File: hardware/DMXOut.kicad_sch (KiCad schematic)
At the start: 3 parts, among them J201 SJ2-25404B-SMT-TR, U201 THVD24x2

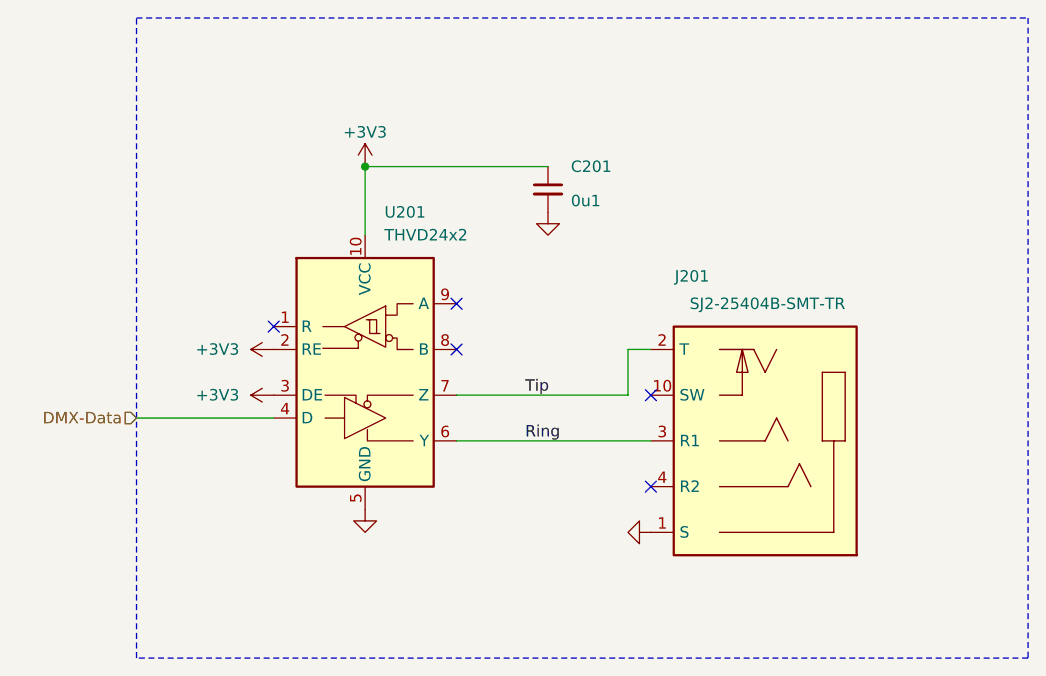
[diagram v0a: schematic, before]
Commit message: Update symbols
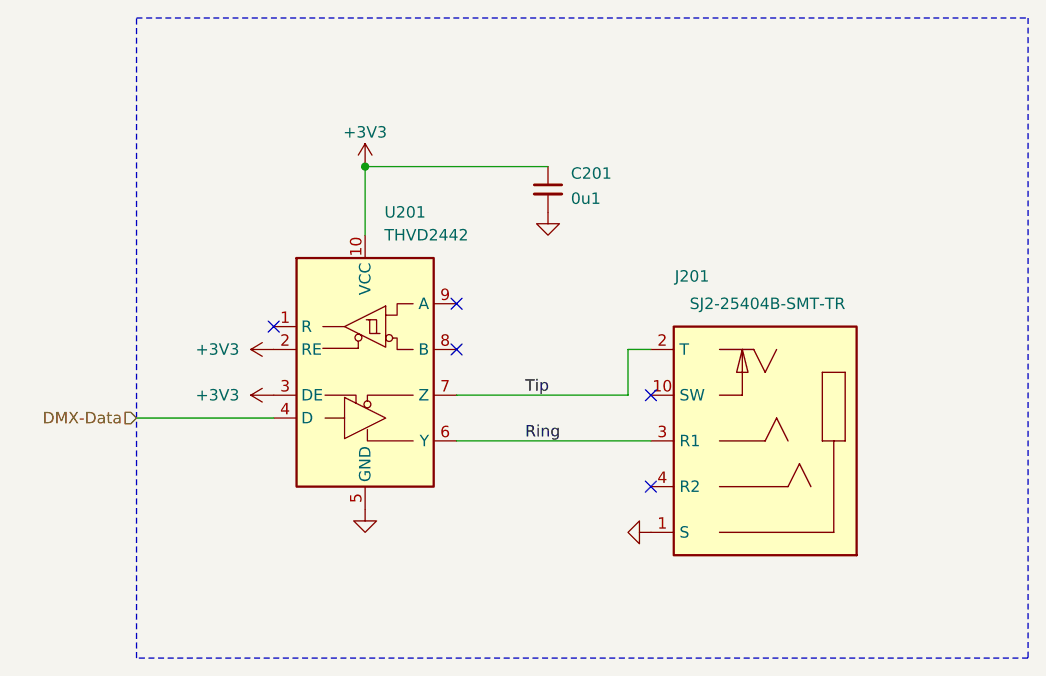
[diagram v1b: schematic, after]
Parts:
- C201: footprint Capacitor_SMD:C_0603_1608Metric -> V2_Capacitor_SMD:C_0603; symbol Device:C_Small -> V2_Device:C_0603_0u1; Mouser (none) -> 810-CGA3E2X7R1H104MA
- J201: Mouser (none) -> 490-SJ2-25404BSMT-TR
- U201: value THVD24x2 -> THVD2442; symbol V2_Interface_RS485:THVD24x2 -> V2_Interface_RS485:THVD2442; Mouser (none) -> 595-THVD2442DRCR
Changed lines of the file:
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@@
 			)
 		)
-		(property "Description" ""
+		(property "Description" "Power symbol creates a global label with name \"GND\" , ground"
 			(at 128.27 125.73 0)
 			(effects
@@
 	)
 	(symbol
-		(lib_id "V2_Interface_RS485:THVD24x2")
+		(lib_id "V2_Interface_RS485:THVD2442")
 		(at 128.27 110.49 0)
 		(unit 1)
@@
 			)
 		)
-		(property "Value" "THVD24x2"
+		(property "Value" "THVD2442"
 			(at 130.4133 95.25 0)
 			(effects
@@
 		)
 		(property "Description" ""
+			(at 128.27 110.49 0)
+			(effects
+				(font
+					(size 1.27 1.27)
+				)
+				(hide yes)
+			)
+		)
+		(property "Mouser" " 595-THVD2442DRCR "
 			(at 128.27 110.49 0)
 			(effects
@@
 			)
 		)
-		(property "Description" ""
+		(property "Description" "Power symbol creates a global label with name \"+3V3\""
 			(at 128.27 87.63 0)
 			(effects
@@
 			)
 		)
-		(property "Description" ""
+		(property "Description" "Power symbol creates a global label with name \"GND\" , ground"
 			(at 160.02 128.27 0)
 			(effects
@@
 			)
 		)
-		(property "Description" ""
+		(property "Description" "Power symbol creates a global label with name \"+3V3\""
 			(at 118.11 107.95 0)
 			(effects
@@
 			)
 		)
+		(property "Mouser" " 490-SJ2-25404BSMT-TR"
+			(at 172.72 118.11 0)
+			(effects
+				(font
+					(size 1.27 1.27)
+				)
+				(hide yes)
+			)
+		)
 		(pin "1"
 		)
@@
 	)
 	(symbol
-		(lib_id "Device:C_Small")
+		(lib_id "V2_Device:C_0603_0u1")
 		(at 148.59 90.17 0)
 		(unit 1)
@@
 		(dnp no)
 		(property "Reference" "C201"
-			(at 151.13 87.6362 0)
+			(at 151.13 88.392 0)
 			(effects
 				(font
@@
 		)
 		(property "Value" "0u1"
-			(at 151.13 91.4462 0)
+			(at 151.13 91.186 0)
 			(effects
 				(font
@@
 			)
 		)
-		(property "Footprint" "Capacitor_SMD:C_0603_1608Metric"
+		(property "Footprint" "V2_Capacitor_SMD:C_0603"
+			(at 148.59 107.188 0)
+			(effects
+				(font
+					(size 1.27 1.27)
+				)
+				(hide yes)
+			)
+		)
+		(property "Datasheet" ""
 			(at 148.59 90.17 0)
 			(effects
@@
 			)
 		)
-		(property "Datasheet" "~"
-			(at 148.59 90.17 0)
-			(effects
-				(font
-					(size 1.27 1.27)
-				)
-				(hide yes)
-			)
-		)
-		(property "Description" ""
-			(at 148.59 90.17 0)
+		(property "Description" "Unpolarized capacitor, small symbol"
+			(at 148.59 103.632 0)
+			(effects
+				(font
+					(size 1.27 1.27)
+				)
+				(hide yes)
+			)
+		)
+		(property "Mouser" " 810-CGA3E2X7R1H104MA"
+			(at 148.59 110.49 0)
 			(effects
 				(font
@@
 			)
 		)
-		(property "Description" ""
+		(property "Description" "Power symbol creates a global label with name \"GND\" , ground"
 			(at 148.59 92.71 0)
 			(effects
@@
 			)
 		)
-		(property "Description" ""
+		(property "Description" "Power symbol creates a global label with name \"+3V3\""
 			(at 118.11 113.03 0)
 			(effects

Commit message: Refresh
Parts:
- C201: Mouser 810-CGA3E2X7R1H104MA -> 810-CGA3E2X7R1H104MA
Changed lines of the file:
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@@
 			)
 		)
-		(property "Mouser" " 810-CGA3E2X7R1H104MA"
+		(property "Mouser" "810-CGA3E2X7R1H104MA"
 			(at 148.59 110.49 0)
 			(effects

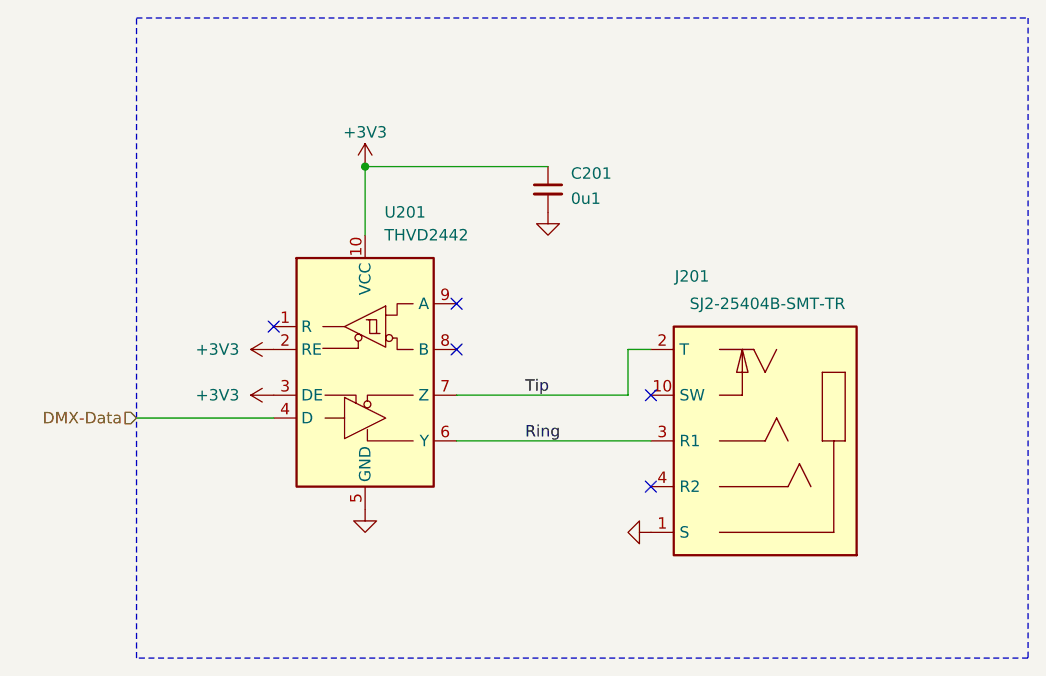
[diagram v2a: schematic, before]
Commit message: Update power symbols
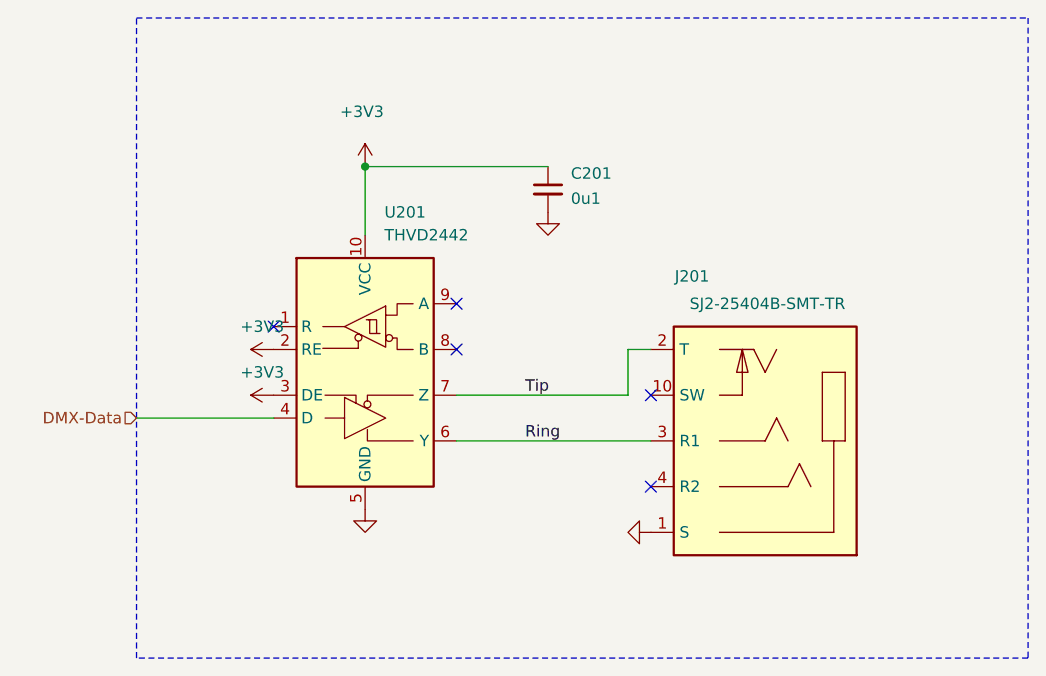
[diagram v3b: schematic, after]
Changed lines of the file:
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@@
 	)
 	(symbol
-		(lib_id "power:GND")
+		(lib_id "V2_power:GND")
 		(at 128.27 125.73 0)
 		(unit 1)
@@
 		)
 		(property "Value" "GND"
-			(at 128.27 130.81 0)
+			(at 128.27 129.794 0)
 			(effects
 				(font
@@
 		)
 		(property "Description" "Power symbol creates a global label with name \"GND\" , ground"
-			(at 128.27 125.73 0)
+			(at 128.016 136.144 0)
 			(effects
 				(font
@@
 	)
 	(symbol
-		(lib_id "power:+3V3")
+		(lib_id "V2_power:+3V3")
 		(at 128.27 87.63 0)
 		(unit 1)
@@
 		(on_board yes)
 		(dnp no)
-		(fields_autoplaced yes)
 		(property "Reference" "#PWR0201"
 			(at 128.27 91.44 0)
@@
 		)
 		(property "Value" "+3V3"
-			(at 128.27 83.82 0)
-			(effects
-				(font
-					(size 1.27 1.27)
-				)
+			(at 125.476 81.534 0)
+			(effects
+				(font
+					(size 1.27 1.27)
+				)
+				(justify left)
 			)
 		)
@@
 		)
 		(property "Description" "Power symbol creates a global label with name \"+3V3\""
-			(at 128.27 87.63 0)
+			(at 128.27 102.616 0)
 			(effects
 				(font
@@
 	)
 	(symbol
-		(lib_id "power:GND")
+		(lib_id "V2_power:GND")
 		(at 160.02 128.27 270)
 		(unit 1)
@@
 		)
 		(property "Value" "GND"
-			(at 156.21 128.2699 90)
-			(effects
-				(font
-					(size 1.27 1.27)
-				)
-				(justify right)
+			(at 155.956 128.27 0)
+			(effects
+				(font
+					(size 1.27 1.27)
+				)
 				(hide yes)
 			)
@@
 		)
 		(property "Description" "Power symbol creates a global label with name \"GND\" , ground"
-			(at 160.02 128.27 0)
+			(at 149.606 128.016 0)
 			(effects
 				(font
@@
 	)
 	(symbol
-		(lib_id "power:+3V3")
+		(lib_id "V2_power:+3V3")
 		(at 118.11 107.95 90)
 		(unit 1)
@@
 		)
 		(property "Value" "+3V3"
-			(at 114.3 107.9499 90)
-			(effects
-				(font
-					(size 1.27 1.27)
-				)
-				(justify left)
+			(at 116.84 105.41 90)
+			(effects
+				(font
+					(size 1.27 1.27)
+				)
 			)
 		)
@@
 		)
 		(property "Description" "Power symbol creates a global label with name \"+3V3\""
-			(at 118.11 107.95 0)
+			(at 133.096 107.95 0)
 			(effects
 				(font
@@
 	)
 	(symbol
-		(lib_id "power:GND")
+		(lib_id "V2_power:GND")
 		(at 148.59 92.71 0)
 		(unit 1)
@@
 		)
 		(property "Value" "GND"
-			(at 148.59 97.79 0)
+			(at 148.59 96.774 0)
 			(effects
 				(font
@@
 		)
 		(property "Description" "Power symbol creates a global label with name \"GND\" , ground"
-			(at 148.59 92.71 0)
+			(at 148.336 103.124 0)
 			(effects
 				(font
@@
 	)
 	(symbol
-		(lib_id "power:+3V3")
+		(lib_id "V2_power:+3V3")
 		(at 118.11 113.03 90)
 		(unit 1)
@@
 		)
 		(property "Value" "+3V3"
-			(at 114.3 113.0299 90)
-			(effects
-				(font
-					(size 1.27 1.27)
-				)
-				(justify left)
+			(at 116.84 110.49 90)
+			(effects
+				(font
+					(size 1.27 1.27)
+				)
 			)
 		)
@@
 		)
 		(property "Description" "Power symbol creates a global label with name \"+3V3\""
-			(at 118.11 113.03 0)
-			(effects
-				(font
+			(at 133.096 113.03 0)
+			(effects
+				(font

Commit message: Update parts
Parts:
- C201: Manufacturer (none) -> TDK; Product (none) -> CGA3E2X7R1H104M080AA
- J201: Manufacturer (none) -> Same Sky; Mouser 490-SJ2-25404BSMT-TR -> 490-SJ2-25404BSMT-TR; Product (none) -> SJ2-25404B-SMT-TR
- U201: Manufacturer (none) -> Texas Instruments; Mouser 595-THVD2442DRCR -> 595-THVD2442DRCR; Product (none) -> THVD2442DRCR
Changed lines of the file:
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@@
 			)
 		)
-		(property "Mouser" " 595-THVD2442DRCR "
+		(property "Mouser" "595-THVD2442DRCR"
 			(at 128.27 110.49 0)
+			(effects
+				(font
+					(size 1.27 1.27)
+				)
+				(hide yes)
+			)
+		)
+		(property "Product" "THVD2442DRCR "
+			(at 128.27 143.51 0)
+			(effects
+				(font
+					(size 1.27 1.27)
+				)
+				(hide yes)
+			)
+		)
+		(property "Manufacturer" "Texas Instruments"
+			(at 128.27 140.97 0)
 			(effects
 				(font
@@
 		)
 		(property "Value" "+3V3"
-			(at 125.476 81.534 0)
+			(at 125.476 82.804 0)
 			(effects
 				(font
@@
 		(on_board yes)
 		(dnp no)
-		(fields_autoplaced yes)
 		(property "Reference" "#PWR0203"
 			(at 121.92 107.95 0)
@@
 		)
 		(property "Value" "+3V3"
-			(at 116.84 105.41 90)
+			(at 111.76 107.95 90)
 			(effects
 				(font
@@
 			)
 		)
-		(property "Mouser" " 490-SJ2-25404BSMT-TR"
+		(property "Mouser" "490-SJ2-25404BSMT-TR"
 			(at 172.72 118.11 0)
+			(effects
+				(font
+					(size 1.27 1.27)
+				)
+				(hide yes)
+			)
+		)
+		(property "Product" "SJ2-25404B-SMT-TR"
+			(at 172.72 82.55 0)
+			(effects
+				(font
+					(size 1.27 1.27)
+				)
+				(hide yes)
+			)
+		)
+		(property "Manufacturer" "Same Sky"
+			(at 172.72 85.09 0)
 			(effects
 				(font
@@
 		(property "Mouser" "810-CGA3E2X7R1H104MA"
 			(at 148.59 110.49 0)
+			(effects
+				(font
+					(size 1.27 1.27)
+				)
+				(hide yes)
+			)
+		)
+		(property "Manufacturer" "TDK"
+			(at 148.59 105.41 0)
+			(effects
+				(font
+					(size 1.27 1.27)
+				)
+				(hide yes)
+			)
+		)
+		(property "Product" "CGA3E2X7R1H104M080AA"
+			(at 148.59 107.95 0)
 			(effects
 				(font
@@
 		(on_board yes)
 		(dnp no)
-		(fields_autoplaced yes)
 		(property "Reference" "#PWR0204"
 			(at 121.92 113.03 0)
@@
 		)
 		(property "Value" "+3V3"
-			(at 116.84 110.49 90)
-			(effects
-				(font
+			(at 111.506 113.03 90)
+			(effects
+				(font

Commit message: Refresh
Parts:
- C201: Rating (none) -> 50V
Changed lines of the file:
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@@
 			)
 		)
-		(property "Description" "Power symbol creates a global label with name \"GND\" , ground"
+		(property "Description" ""
 			(at 128.016 136.144 0)
 			(effects
@@
 			)
 		)
-		(property "Description" "Power symbol creates a global label with name \"+3V3\""
+		(property "Description" ""
 			(at 128.27 102.616 0)
 			(effects
@@
 			)
 		)
-		(property "Description" "Power symbol creates a global label with name \"GND\" , ground"
+		(property "Description" ""
 			(at 149.606 128.016 0)
 			(effects
@@
 			)
 		)
-		(property "Description" "Power symbol creates a global label with name \"+3V3\""
+		(property "Description" ""
 			(at 133.096 107.95 0)
 			(effects
@@
 		(property "Product" "CGA3E2X7R1H104M080AA"
 			(at 148.59 107.95 0)
+			(effects
+				(font
+					(size 1.27 1.27)
+				)
+				(hide yes)
+			)
+		)
+		(property "Rating" "50V"
+			(at 148.59 113.03 0)
 			(effects
 				(font
@@
 			)
 		)
-		(property "Description" "Power symbol creates a global label with name \"GND\" , ground"
+		(property "Description" ""
 			(at 148.336 103.124 0)
 			(effects
@@
 			)
 		)
-		(property "Description" "Power symbol creates a global label with name \"+3V3\""
+		(property "Description" ""
 			(at 133.096 113.03 0)
 			(effects

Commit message: Update Library
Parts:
- C201: symbol V2_Device:C_0603_0u1 -> V2_Capacitor:0603_0u1
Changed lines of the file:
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@@
 		(dnp no)
 		(fields_autoplaced yes)
-		(property "Reference" "#PWR0205"
+		(property "Reference" "#PWR205"
 			(at 128.27 132.08 0)
 			(effects
@@
 			(project "dmx"
 				(path "/6c8448b4-b04d-47e1-934e-e40cbe27a7be/1b21f4b2-19b6-442e-b6c3-9ab356361c9a"
-					(reference "#PWR0205")
+					(reference "#PWR205")
 					(unit 1)
 				)
@@
 		(on_board yes)
 		(dnp no)
-		(property "Reference" "#PWR0201"
+		(property "Reference" "#PWR201"
 			(at 128.27 91.44 0)
 			(effects
@@
 			(project "dmx"
 				(path "/6c8448b4-b04d-47e1-934e-e40cbe27a7be/1b21f4b2-19b6-442e-b6c3-9ab356361c9a"
-					(reference "#PWR0201")
+					(reference "#PWR201")
 					(unit 1)
 				)
@@
 		(dnp no)
 		(fields_autoplaced yes)
-		(property "Reference" "#PWR0206"
+		(property "Reference" "#PWR206"
 			(at 153.67 128.27 0)
 			(effects
@@
 			(project "dmx"
 				(path "/6c8448b4-b04d-47e1-934e-e40cbe27a7be/1b21f4b2-19b6-442e-b6c3-9ab356361c9a"
-					(reference "#PWR0206")
+					(reference "#PWR206")
 					(unit 1)
 				)
@@
 		(on_board yes)
 		(dnp no)
-		(property "Reference" "#PWR0203"
+		(property "Reference" "#PWR203"
 			(at 121.92 107.95 0)
 			(effects
@@
 			(project "dmx"
 				(path "/6c8448b4-b04d-47e1-934e-e40cbe27a7be/1b21f4b2-19b6-442e-b6c3-9ab356361c9a"
-					(reference "#PWR0203")
+					(reference "#PWR203")
 					(unit 1)
 				)
@@
 	)
 	(symbol
-		(lib_id "V2_Device:C_0603_0u1")
+		(lib_id "V2_Capacitor:0603_0u1")
 		(at 148.59 90.17 0)
 		(unit 1)
@@
 		(dnp no)
 		(fields_autoplaced yes)
-		(property "Reference" "#PWR0202"
+		(property "Reference" "#PWR202"
 			(at 148.59 99.06 0)
 			(effects
@@
 			(project "dmx"
 				(path "/6c8448b4-b04d-47e1-934e-e40cbe27a7be/1b21f4b2-19b6-442e-b6c3-9ab356361c9a"
-					(reference "#PWR0202")
+					(reference "#PWR202")
 					(unit 1)
 				)
@@
 		(on_board yes)
 		(dnp no)
-		(property "Reference" "#PWR0204"
+		(property "Reference" "#PWR204"
 			(at 121.92 113.03 0)
 			(effects
@@
 			(project "dmx"
 				(path "/6c8448b4-b04d-47e1-934e-e40cbe27a7be/1b21f4b2-19b6-442e-b6c3-9ab356361c9a"
-					(reference "#PWR0204")
-					(unit 1)
-				)
+					(reference "#PWR204")
+					(unit 1)
+				)
